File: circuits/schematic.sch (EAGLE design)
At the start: 42 parts, among them IC1 MEGA8-P, IC2 MAX481CPA, J1 AVR_SPI_PRG_6PTH

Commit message: Self routed version.
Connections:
- net GND: now also JP5.1; no longer JP5.2
- net VCC: now also JP5.2; no longer JP5.1
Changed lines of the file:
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@@
 <grid distance="0.1" unitdist="inch" unit="inch" style="lines" multiple="1" display="no" altdistance="0.01" altunitdist="inch" altunit="inch"/>
 <layers>
-<layer number="1" name="Top" color="4" fill="1" visible="yes" active="no"/>
-<layer number="16" name="Bottom" color="1" fill="1" visible="yes" active="no"/>
-<layer number="17" name="Pads" color="2" fill="1" visible="yes" active="no"/>
-<layer number="18" name="Vias" color="2" fill="1" visible="yes" active="no"/>
-<layer number="19" name="Unrouted" color="6" fill="1" visible="yes" active="no"/>
-<layer number="20" name="Dimension" color="15" fill="1" visible="yes" active="no"/>
-<layer number="21" name="tPlace" color="7" fill="1" visible="yes" active="no"/>
-<layer number="22" name="bPlace" color="7" fill="1" visible="yes" active="no"/>
-<layer number="23" name="tOrigins" color="15" fill="1" visible="yes" active="no"/>
-<layer number="24" name="bOrigins" color="15" fill="1" visible="yes" active="no"/>
-<layer number="25" name="tNames" color="7" fill="1" visible="yes" active="no"/>
-<layer number="26" name="bNames" color="7" fill="1" visible="yes" active="no"/>
-<layer number="27" name="tValues" color="7" fill="1" visible="yes" active="no"/>
-<layer number="28" name="bValues" color="7" fill="1" visible="yes" active="no"/>
+<layer number="1" name="Top" color="4" fill="1" visible="no" active="no"/>
+<layer number="16" name="Bottom" color="1" fill="1" visible="no" active="no"/>
+<layer number="17" name="Pads" color="2" fill="1" visible="no" active="no"/>
+<layer number="18" name="Vias" color="2" fill="1" visible="no" active="no"/>
+<layer number="19" name="Unrouted" color="6" fill="1" visible="no" active="no"/>
+<layer number="20" name="Dimension" color="15" fill="1" visible="no" active="no"/>
+<layer number="21" name="tPlace" color="7" fill="1" visible="no" active="no"/>
+<layer number="22" name="bPlace" color="7" fill="1" visible="no" active="no"/>
+<layer number="23" name="tOrigins" color="15" fill="1" visible="no" active="no"/>
+<layer number="24" name="bOrigins" color="15" fill="1" visible="no" active="no"/>
+<layer number="25" name="tNames" color="7" fill="1" visible="no" active="no"/>
+<layer number="26" name="bNames" color="7" fill="1" visible="no" active="no"/>
+<layer number="27" name="tValues" color="7" fill="1" visible="no" active="no"/>
+<layer number="28" name="bValues" color="7" fill="1" visible="no" active="no"/>
 <layer number="29" name="tStop" color="7" fill="3" visible="no" active="no"/>
 <layer number="30" name="bStop" color="7" fill="6" visible="no" active="no"/>
@@
 <layer number="35" name="tGlue" color="7" fill="4" visible="no" active="no"/>
 <layer number="36" name="bGlue" color="7" fill="5" visible="no" active="no"/>
-<layer number="37" name="tTest" color="7" fill="1" visible="yes" active="no"/>
-<layer number="38" name="bTest" color="7" fill="1" visible="yes" active="no"/>
+<layer number="37" name="tTest" color="7" fill="1" visible="no" active="no"/>
+<layer number="38" name="bTest" color="7" fill="1" visible="no" active="no"/>
 <layer number="39" name="tKeepout" color="4" fill="11" visible="no" active="no"/>
 <layer number="40" name="bKeepout" color="1" fill="11" visible="no" active="no"/>
@@
 <layer number="44" name="Drills" color="7" fill="1" visible="no" active="no"/>
 <layer number="45" name="Holes" color="7" fill="1" visible="no" active="no"/>
-<layer number="46" name="Milling" color="3" fill="1" visible="yes" active="no"/>
-<layer number="47" name="Measures" color="7" fill="1" visible="yes" active="no"/>
-<layer number="48" name="Document" color="7" fill="1" visible="yes" active="no"/>
-<layer number="49" name="Reference" color="7" fill="1" visible="yes" active="no"/>
-<layer number="50" name="dxf" color="7" fill="1" visible="yes" active="no"/>
-<layer number="51" name="tDocu" color="7" fill="1" visible="yes" active="no"/>
-<layer number="52" name="bDocu" color="7" fill="1" visible="yes" active="no"/>
-<layer number="53" name="tGND_GNDA" color="7" fill="9" visible="yes" active="no"/>
-<layer number="54" name="bGND_GNDA" color="1" fill="9" visible="yes" active="no"/>
-<layer number="56" name="wert" color="7" fill="1" visible="yes" active="no"/>
+<layer number="46" name="Milling" color="3" fill="1" visible="no" active="no"/>
+<layer number="47" name="Measures" color="7" fill="1" visible="no" active="no"/>
+<layer number="48" name="Document" color="7" fill="1" visible="no" active="no"/>
+<layer number="49" name="Reference" color="7" fill="1" visible="no" active="no"/>
+<layer number="50" name="dxf" color="7" fill="1" visible="no" active="no"/>
+<layer number="51" name="tDocu" color="7" fill="1" visible="no" active="no"/>
+<layer number="52" name="bDocu" color="7" fill="1" visible="no" active="no"/>
+<layer number="53" name="tGND_GNDA" color="7" fill="9" visible="no" active="no"/>
+<layer number="54" name="bGND_GNDA" color="1" fill="9" visible="no" active="no"/>
+<layer number="56" name="wert" color="7" fill="1" visible="no" active="no"/>
 <layer number="91" name="Nets" color="2" fill="1" visible="yes" active="yes"/>
 <layer number="92" name="Busses" color="1" fill="1" visible="yes" active="yes"/>
@@
 <instance part="JP5" gate="G$1" x="48.26" y="-27.94"/>
 <instance part="R1" gate="G$1" x="-5.08" y="88.9" rot="R270"/>
-<instance part="GND1" gate="1" x="58.42" y="-25.4" rot="R90"/>
+<instance part="GND1" gate="1" x="58.42" y="-27.94" rot="R90"/>
 <instance part="GND2" gate="1" x="20.32" y="43.18" rot="R270"/>
-<instance part="P+4" gate="VCC" x="58.42" y="-27.94" rot="R270"/>
+<instance part="P+4" gate="VCC" x="58.42" y="-25.4" rot="R270"/>
 <instance part="P+6" gate="VCC" x="20.32" y="38.1" rot="R90"/>
 <instance part="P+8" gate="VCC" x="-5.08" y="96.52"/>
@@
 <net name="VCC" class="0">
 <segment>
-<pinref part="JP5" gate="G$1" pin="1"/>
-<pinref part="P+4" gate="VCC" pin="VCC"/>
-</segment>
-<segment>
 <pinref part="IC1" gate="G$1" pin="VCC@1"/>
 <pinref part="P+6" gate="VCC" pin="VCC"/>
@@
 <pinref part="P+11" gate="VCC" pin="VCC"/>
 </segment>
+<segment>
+<pinref part="JP5" gate="G$1" pin="2"/>
+<pinref part="P+4" gate="VCC" pin="VCC"/>
+</segment>
 </net>
 <net name="GND" class="0">
-<segment>
-<pinref part="JP5" gate="G$1" pin="2"/>
-<pinref part="GND1" gate="1" pin="GND"/>
-</segment>
 <segment>
 <pinref part="IC1" gate="G$1" pin="GND@1"/>
@@
 <pinref part="GND22" gate="1" pin="GND"/>
 </segment>
-</net>
+<segment>
+<pinref part="JP5" gate="G$1" pin="1"/>
+<pinref part="GND1" gate="1" pin="GND"/>
+</segment>
+</net>

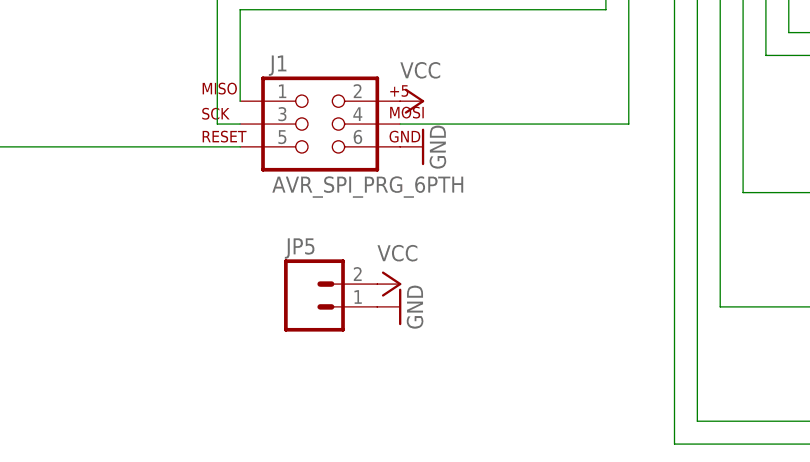
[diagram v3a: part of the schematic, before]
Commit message: Fix RJ45 jack footprint.
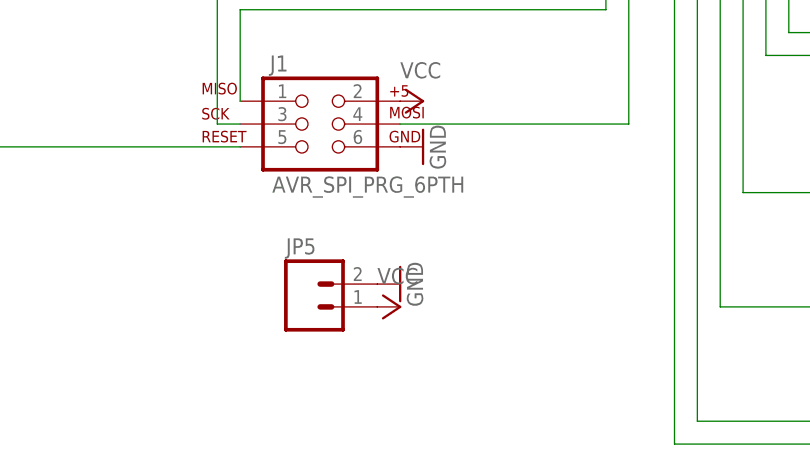
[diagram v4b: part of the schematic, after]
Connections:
- net GND: now also JP5.2; no longer JP5.1
- net VCC: now also JP5.1; no longer JP5.2
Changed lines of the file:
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@@
 <instance part="JP5" gate="G$1" x="48.26" y="-27.94"/>
 <instance part="R1" gate="G$1" x="-5.08" y="88.9" rot="R270"/>
-<instance part="GND1" gate="1" x="58.42" y="-27.94" rot="R90"/>
+<instance part="GND1" gate="1" x="58.42" y="-25.4" rot="R90"/>
 <instance part="GND2" gate="1" x="20.32" y="43.18" rot="R270"/>
-<instance part="P+4" gate="VCC" x="58.42" y="-25.4" rot="R270"/>
+<instance part="P+4" gate="VCC" x="58.42" y="-27.94" rot="R270"/>
 <instance part="P+6" gate="VCC" x="20.32" y="38.1" rot="R90"/>
 <instance part="P+8" gate="VCC" x="-5.08" y="96.52"/>
@@
 </segment>
 <segment>
-<pinref part="JP5" gate="G$1" pin="2"/>
+<pinref part="JP5" gate="G$1" pin="1"/>
 <pinref part="P+4" gate="VCC" pin="VCC"/>
 </segment>
@@
 </segment>
 <segment>
-<pinref part="JP5" gate="G$1" pin="1"/>
+<pinref part="JP5" gate="G$1" pin="2"/>
 <pinref part="GND1" gate="1" pin="GND"/>
 </segment>
